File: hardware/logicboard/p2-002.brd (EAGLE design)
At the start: 72 x 72 mm, 20 parts, among them IC1 74LS07N, U1 DS18B20

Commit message: DIP SW.
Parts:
- added S1, S2: (no value), switch-dil:A1353HEX
- moved C9 33.0 mm to (51.5, 8.00)
- moved D3 32.8 mm to (23.0, 45.8)
- moved RN1 31.9 mm to (23.0, 26.2)
- moved C8 24.5 mm to (51.5, 30.0)
- moved IC1 11.0 mm to (51.5, 19.0)
- moved OK1 10.0 mm to (51.5, 38.0)
- moved RN3 1.00 mm to (36.0, 61.0)
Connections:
- net ANLG1: now also S2.1
- net ANLG2: now also S2.2
- net ANLG3: now also S2.4
- net ANLG4: now also S2.8
- net DTCT1: now also S1.1
- net DTCT2: now also S1.2
- net DTCT3: now also S1.4
- net DTCT4: now also S1.8
- net GND: now also S1.C, S2.C
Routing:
- net ANLG1: track 37.4 -> 94.0 mm, vias 0 -> 1
- net ANLG2: track 36.4 -> 90.5 mm
- net ANLG4: track 30.2 -> 79.1 mm, vias 0 -> 2
- net DTCT2: track 59.9 -> 108.6 mm, vias 1 -> 0
- net MO2: track 35.8 -> 80.9 mm
- net ANLG3: track 31.2 -> 72.7 mm, vias 0 -> 1
- net GND: track 256.2 -> 288.5 mm, vias 2 -> 1
- net VIN: track 107.8 -> 137.7 mm, vias 2 -> 0
- net VCC: track 198.5 -> 226.7 mm, vias 2 -> 3
- net DTCT1: track 52.7 -> 78.9 mm, vias 1 -> 3
- net DTCT3: track 67.4 -> 92.6 mm
- net DTCT4: track 68.6 -> 90.5 mm, vias 1 -> 0
- net MIRTN: track 79.1 -> 63.3 mm, vias 1 -> 0
- net MO: track 32.9 -> 44.4 mm, vias 0 -> 1
- net MT: track 28.9 -> 40.1 mm
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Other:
- board text added: "1"
- board text added: "1(8)"
- board text added: "2"
- board text added: "2(4)"
- board text added: "3"
- board text added: "4"
- board text added: "4(2)"
- board text added: "8(1)"
- board text added: "Bit # of JAE (Omron)"
- board text added: "Connected pin #"

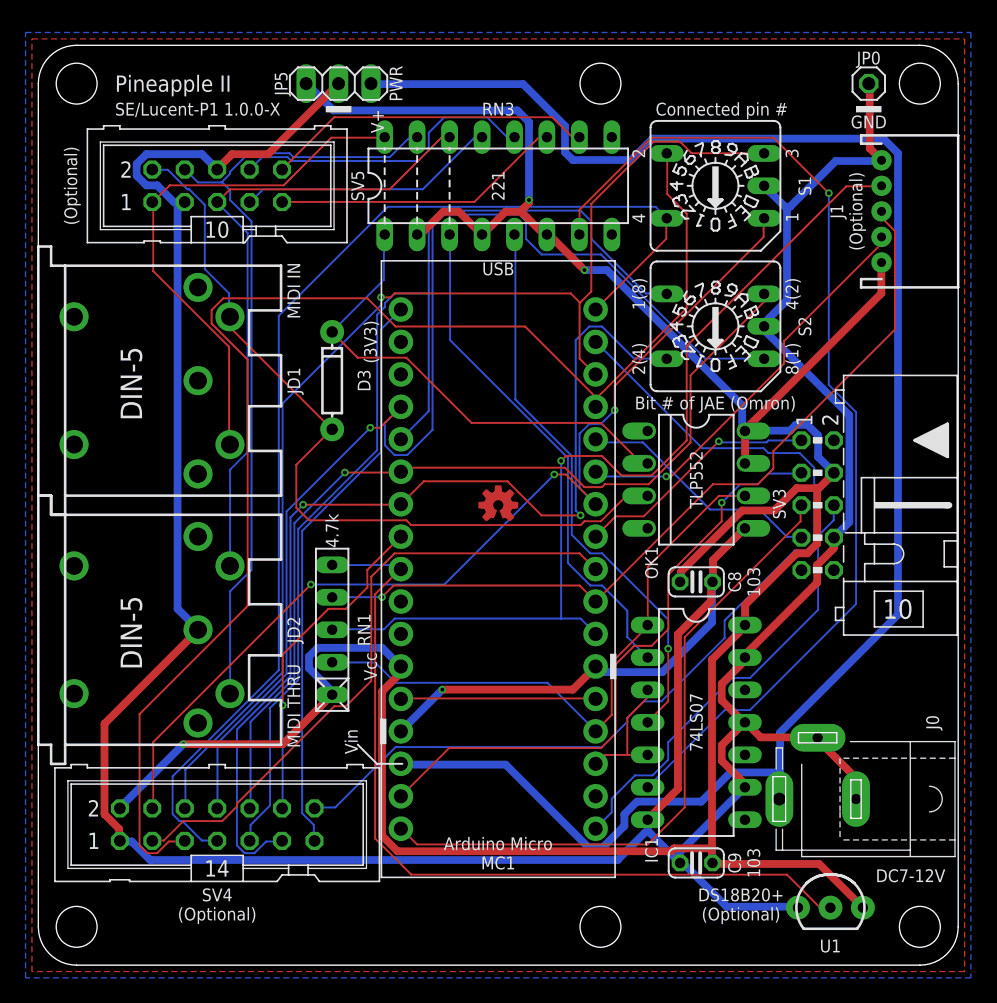
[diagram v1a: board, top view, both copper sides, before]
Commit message: Removed PWR pins.
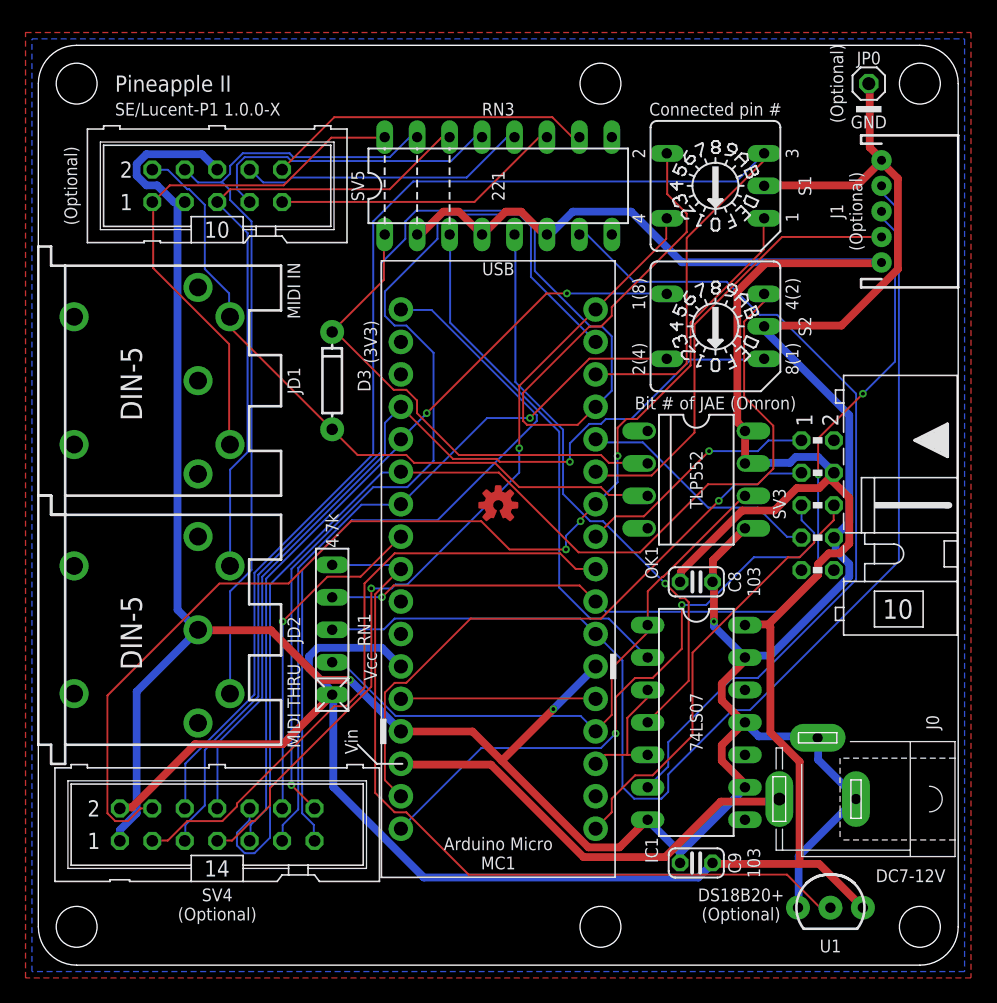
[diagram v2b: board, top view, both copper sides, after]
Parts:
- removed JP5: D5V, pinhead:1X03
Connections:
- net GND: no longer JP5.2
- net VCC: no longer JP5.1
- net VIN: no longer JP5.3
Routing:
- net VIN: track 137.7 -> 34.5 mm
- net GND: track 288.5 -> 251.4 mm, vias 1 -> 3
- net ANLG2: track 90.5 -> 61.9 mm, vias 0 -> 2
- net DTCT4: track 90.5 -> 65.6 mm, vias 0 -> 2
- net ANLG1: track 94.0 -> 71.8 mm
- net ANLG4: track 79.1 -> 57.5 mm, vias 2 -> 1
- net SDA: track 73.5 -> 94.8 mm, vias 1 -> 0
- net DTCT3: track 92.6 -> 111.3 mm, vias 1 -> 0
- net ANLG3: track 72.7 -> 90.1 mm, vias 1 -> 0
- net MO2: track 80.9 -> 65.6 mm, vias 1 -> 0
- net LED0: track 45.2 -> 59.3 mm
- net VCC: track 226.7 -> 214.3 mm, vias 3 -> 0
- net DTCT1: track 78.9 -> 88.7 mm
- net DTCT2: track 108.6 -> 118.2 mm
- net MIRTN: track 63.3 -> 53.8 mm
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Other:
- board text removed: "PWR"
- board text removed: "V+"
